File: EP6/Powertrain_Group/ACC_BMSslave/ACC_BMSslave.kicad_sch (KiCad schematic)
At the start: 99 parts, among them IC1 ADBMS1818ASWAZ-R7, J1 Cell taps, J2 Temp probes A, J3 Temp probes B, J4 Temp probes C, J5 Temp probes D, J6 RJ45, J7 RJ45, J8 isoSPI_out, J9 isoSPI_in, U1 LM324DT

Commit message: ACC_BMSslave pcb priliminary layout
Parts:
- C1, C10, C11, C12, C13, C2, C3, C4, C7, C8, C9: footprint Capacitor_SMD:C_0201_0603Metric -> Capacitor_SMD:C_0603_1608Metric
- D1, D2: footprint LED_SMD:LED_0805_2012Metric -> LED_SMD:LED_0603_1608Metric
- R1, R10, R11, R12, R13, R14, R15, R16, R17, R18, R19, R2, R20, R21, R22, R23, R24, R25, R26, R27, R28, R29, R3, R30, R31, R32, R33, R34, R35, R36, R37, R38, R4, R5, R6, R7, R8, R9: footprint Resistor_SMD:R_0603_1608Metric -> Resistor_SMD:R_0402_1005Metric
- U1: footprint Package_SO:SOIC-14-16_3.9x9.9mm_P1.27mm -> Package_SO:SO-14_3.9x8.65mm_P1.27mm
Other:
- note added: "A2,A1,A0 000: T8 001: T7 010: T6 011: T5 100: T1 101: T2 110: T3 111: T4"

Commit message: ACC_BMSslave pcb layout kinda done
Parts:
- removed J1: Cell taps, Connector_JST:JST_XH_B16B-XH-A_1x16_P2.50mm_Vertical, symbol Connector_Generic:Conn_01x16
- added J1: Cell taps A, Connector_JST:JST_XH_B8B-XH-A_1x08_P2.50mm_Vertical, symbol Connector_Generic:Conn_01x08
- added J10: Cell taps B, Connector_JST:JST_XH_B8B-XH-A_1x08_P2.50mm_Vertical, symbol Connector_Generic:Conn_01x08
- C10, C11, C14, C15, C8, C9: footprint Capacitor_SMD:C_0603_1608Metric -> Capacitor_SMD:C_0402_1005Metric
- R33: footprint Resistor_SMD:R_0402_1005Metric -> Resistor_SMD:R_0805_2012Metric
- R34: footprint Resistor_SMD:R_0402_1005Metric -> Resistor_SMD:R_0603_1608Metric
- R39, R46, R47: footprint Resistor_SMD:R_0201_0603Metric -> Resistor_SMD:R_0603_1608Metric
- R40, R41, R42, R43, R44, R45, R48, R49: footprint Resistor_SMD:R_0201_0603Metric -> Resistor_SMD:R_0402_1005Metric
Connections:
- net Earth: now also D1.1 (K); no longer R39.2
- net GPIO6: now also C10.1, R42.2; no longer C8.1, R40.2
- net GPIO7: now also C11.1, R43.2; no longer C9.1, R41.2
- net GPIO8: now also C8.1, R40.2; no longer C10.1, R42.2
- net GPIO9: now also C9.1, R41.2; no longer C11.1, R43.2
- net VREG: now also R39.2; no longer D1.2 (A)
- net tprobe_mux2/OUT: now also U1.12 (+); no longer U1.5 (+)
- net tprobe_mux4/OUT: now also U1.5 (+); no longer U1.12 (+)
- net at F6.1: now also J1.6 (Pin_6)
- net at F10.1: now also J10.2 (Pin_2)
- net at F7.1: now also J1.7 (Pin_7)
- net at F5.1: now also J1.5 (Pin_5)
- net at U1.6 (-), U1.7: now also R43.1; no longer R41.1
- net at F4.1: now also J1.4 (Pin_4)
- net at R39.1: now also D1.2 (A); no longer D1.1 (K)
- net at U1.13 (-), U1.14: now also R41.1; no longer R43.1
- net at F13.1: now also J10.5 (Pin_5)
- net at F11.1: now also J10.3 (Pin_3)
- net at F14.1: now also J10.6 (Pin_6)
- net at F1.1: now also J1.1 (Pin_1)
- net at F12.1: now also J10.4 (Pin_4)
- net at F15.1: now also J10.7 (Pin_7)
- net at F16.1: now also J10.8 (Pin_8)
- net at F2.1: now also J1.2 (Pin_2)
- net at F3.1: now also J1.3 (Pin_3)
- net at F8.1: now also J1.8 (Pin_8)
- net at F9.1: now also J10.1 (Pin_1)
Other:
- moved on the sheet: D1, R39, U1B, U1D

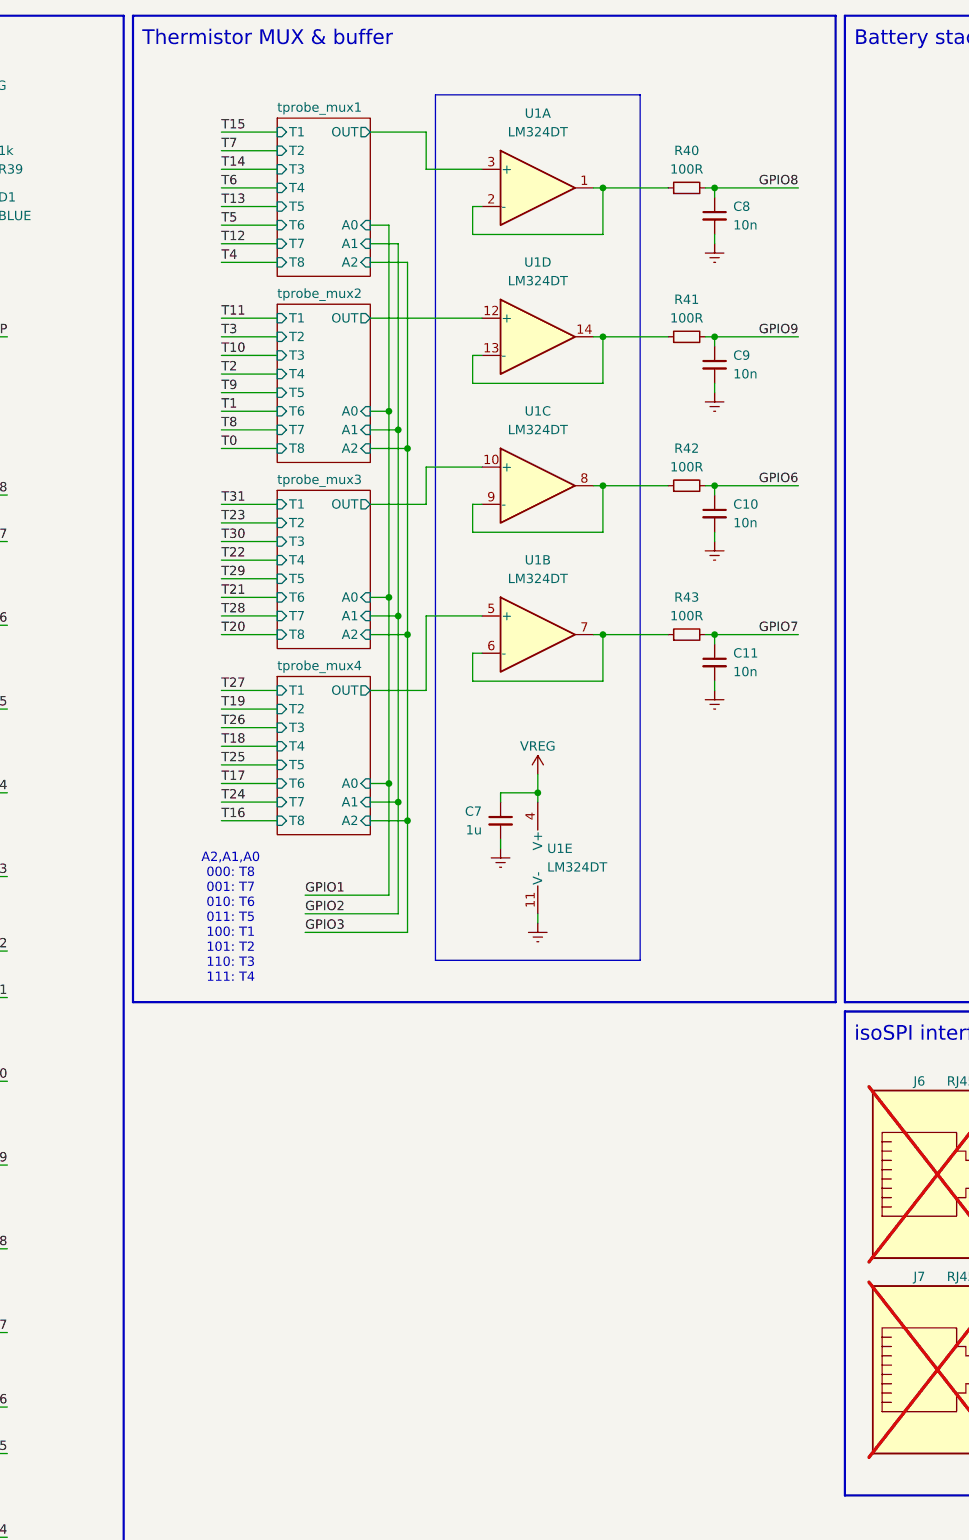
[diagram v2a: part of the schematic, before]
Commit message: ACC_BMSslave optimise layout, added silk
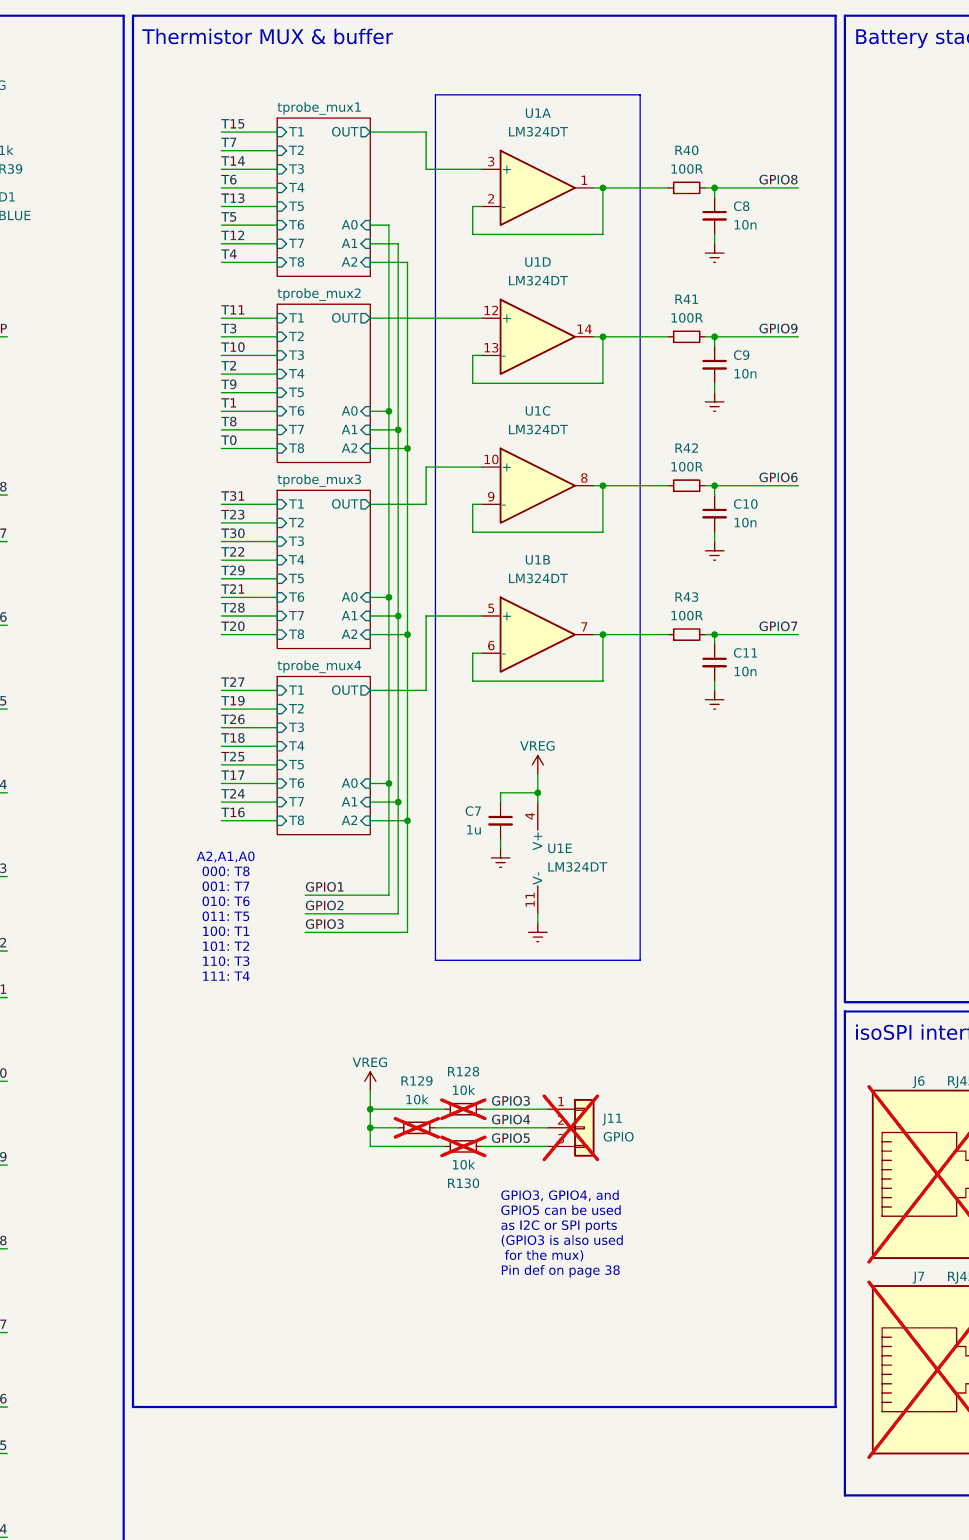
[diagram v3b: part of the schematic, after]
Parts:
- added J11: GPIO, Connector_PinHeader_2.54mm:PinHeader_1x03_P2.54mm_Vertical, symbol Connector_Generic:Conn_01x03
- added R128, R129, R130: 10k, Resistor_SMD:R_0402_1005Metric, symbol Device:R_Small
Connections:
- net GPIO3: now also J11.1 (Pin_1), R128.2
- net GPIO4: now also J11.2 (Pin_2), R129.2
- net GPIO5: now also J11.3 (Pin_3), R130.2
- net VREG: now also R128.1, R129.1, R130.1
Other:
- note added: "GPIO3, GPIO4, and GPIO5 can be used as I2C or SPI ports (GPIO3 is also used for the mux) Pin def on page 38"

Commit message: ACC_BMSslave snapshot
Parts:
- removed D1: BLUE, LED_SMD:LED_0603_1608Metric, symbol Device:LED_Small
- removed J1: Cell taps A, Connector_JST:JST_XH_B8B-XH-A_1x08_P2.50mm_Vertical, symbol Connector_Generic:Conn_01x08
- removed J10: Cell taps B, Connector_JST:JST_XH_B8B-XH-A_1x08_P2.50mm_Vertical, symbol Connector_Generic:Conn_01x08
- removed R31, R32: 10k, Resistor_SMD:R_0402_1005Metric, symbol Device:R_Small
- removed R39: 1k, Resistor_SMD:R_0603_1608Metric, symbol Device:R_Small
- added C26, C57, C58: 10n, Capacitor_SMD:C_0402_1005Metric, symbol Device:C_Small
- added J1: Cell Taps A, Connector_JST:JST_XH_B4B-XH-A_1x04_P2.50mm_Vertical, symbol Connector_Generic:Conn_01x04
- added J10: Cell Taps B, Connector_JST:JST_XH_B4B-XH-A_1x04_P2.50mm_Vertical, symbol Connector_Generic:Conn_01x04
- added J12: Cell Taps C, Connector_JST:JST_XH_B4B-XH-A_1x04_P2.50mm_Vertical, symbol Connector_Generic:Conn_01x04
- added J13: Cell Taps D, Connector_JST:JST_XH_B4B-XH-A_1x04_P2.50mm_Vertical, symbol Connector_Generic:Conn_01x04
- added R131, R132: 100k, Resistor_SMD:R_0402_1005Metric, symbol Device:R_Small
- added R133, R134: 100R, Resistor_SMD:R_0402_1005Metric, symbol Device:R_Small
- added U2: LM324DT, Package_SO:SO-14_3.9x8.65mm_P1.27mm, symbol Amplifier_Operational:LM324
- C11: value 10n -> 1u; footprint Capacitor_SMD:C_0402_1005Metric -> Capacitor_SMD:C_0603_1608Metric
- H1, H2, H3, H4: footprint MountingHole:MountingHole_4.3mm_M4_DIN965 -> MountingHole:MountingHole_3.2mm_M3_DIN965
- R1, R10, R11, R12, R13, R14, R15, R16, R17, R18, R19, R2, R20, R21, R22, R23, R24, R25, R26, R27, R28, R29, R3, R30, R4, R5, R6, R7, R8, R9: value 10k -> 4k3
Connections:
- net T30 is gone; now on net T28: J5.13 (Pin_13)
- net T31 is gone; now on net T29: J5.15 (Pin_15)
- net Earth: now also C26.2, C57.2, C58.2, R131.1, U2.11 (V-)
- net GPIO1: now also C8.1, R40.2
- net GPIO2: now also C9.1, R41.2
- net GPIO7: now also C26.1; no longer C11.1
- net GPIO8: now also C57.1, R133.2; no longer C8.1, R40.2
- net GPIO9: now also C58.1, R134.2; no longer C9.1, R41.2
- net T15: now also J4.1 (Pin_1); no longer J3.15 (Pin_15)
- net T16: now also J4.3 (Pin_3); no longer J4.1 (Pin_1)
- net T17: now also J4.5 (Pin_5); no longer J4.3 (Pin_3)
- net T18: now also J4.7 (Pin_7); no longer J4.5 (Pin_5)
- net T19: now also J4.9 (Pin_9); no longer J4.7 (Pin_7)
- net T20: now also J4.11 (Pin_11); no longer J4.9 (Pin_9)
- net T21: now also J4.13 (Pin_13); no longer J4.11 (Pin_11)
- net T22: now also J5.1 (Pin_1); no longer J4.13 (Pin_13)
- net T23: now also J5.3 (Pin_3); no longer J4.15 (Pin_15)
- net T24: now also J5.5 (Pin_5); no longer J5.1 (Pin_1)
- net T25: now also J5.7 (Pin_7); no longer J5.3 (Pin_3)
- net T26: now also J5.9 (Pin_9); no longer J5.5 (Pin_5)
- net T27: now also J5.11 (Pin_11); no longer J5.7 (Pin_7)
- net T28: no longer J5.9 (Pin_9)
- net T29: no longer J5.11 (Pin_11)
- net VREG: now also C11.1, R132.2, U2.4 (V+)
- net tprobe_mux4/OUT: now also U2.3 (+); no longer U1.5 (+)
- net at F6.1: now also J10.2 (Pin_2)
- net at F10.1: now also J12.2 (Pin_2)
- net at F7.1: now also J10.3 (Pin_3)
- net at F9.1: now also J12.1 (Pin_1)
- net at F11.1: now also J12.3 (Pin_3)
- net at F12.1: now also J12.4 (Pin_4)
- net at F13.1: now also J13.1 (Pin_1)
- net at F14.1: now also J13.2 (Pin_2)
- net at F15.1: now also J13.3 (Pin_3)
- net at F16.1: now also J13.4 (Pin_4)
- net at F5.1: now also J10.1 (Pin_1)
- net at U1.6 (-), U1.7: no longer R43.1
- net at F4.1: now also J1.4 (Pin_4)
- net at F3.1: now also J1.3 (Pin_3)
- net at F8.1: now also J10.4 (Pin_4)
- net at F1.1: now also J1.1 (Pin_1)
- net at F2.1: now also J1.2 (Pin_2)
- new net: R133.1, U2.13 (-), U2.14
- new net: U2.6 (-), U2.7
- new net: R134.1, U2.8, U2.9 (-)
- new net: R43.1, U2.1, U2.2 (-)
- new net mid_supply: R131.2, R132.1, U1.5 (+), U2.5 (+)
- new net tprobe_mux5/OUT: U2.12 (+)
- new net tprobe_mux6/OUT: U2.10 (+)
- no-connect marks 19 -> 39
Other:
- added sheet tprobe_mux5 (tprobe_mux.kicad_sch)
- added sheet tprobe_mux6 (tprobe_mux.kicad_sch)
- note added: "GPIO3, GPIO4, and GPIO5 can be used as I2C or SPI ports Pin def on page 38"
- note removed: "GPIO3, GPIO4, and GPIO5 can be used as I2C or SPI ports (GPIO3 is also used for the mux) Pin def on page 38"
- moved on the sheet: C7, J11, R128, R129, R130, R16, R17, R18, R19, R20, R21, R22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

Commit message: ACC_BMSslave snapshot
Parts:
- removed C11: 1u, Capacitor_SMD:C_0603_1608Metric, symbol Device:C_Small
- removed C26, C58: 10n, Capacitor_SMD:C_0402_1005Metric, symbol Device:C_Small
- removed R131, R132: 100k, Resistor_SMD:R_0402_1005Metric, symbol Device:R_Small
- removed R133, R134, R43: 100R, Resistor_SMD:R_0402_1005Metric, symbol Device:R_Small
- removed U2: LM324DT, Package_SO:SO-14_3.9x8.65mm_P1.27mm, symbol Amplifier_Operational:LM324
- added R31, R32: 4k3, Resistor_SMD:R_0402_1005Metric, symbol Device:R_Small
- added R39: 100R, Resistor_SMD:R_0402_1005Metric, symbol Device:R_Small
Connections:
- net mid_supply is gone; now on net tprobe_mux4/OUT: U1.5 (+)
- net GPIO1: no longer C8.1, R40.2
- net GPIO2: no longer C9.1, R41.2
- net GPIO6: now also C8.1, R40.2; no longer C10.1, R42.2
- net GPIO7: now also C9.1, R41.2
- net GPIO8: now also R39.2
- net GPIO9: now also C10.1, R42.2
- net T15: now also J3.15 (Pin_15); no longer J4.1 (Pin_1)
- net T16: now also J4.1 (Pin_1); no longer J4.3 (Pin_3)
- net T17: now also J4.3 (Pin_3); no longer J4.5 (Pin_5)
- net T18: now also J4.5 (Pin_5); no longer J4.7 (Pin_7)
- net T19: now also J4.7 (Pin_7); no longer J4.9 (Pin_9)
- net T20: now also J4.9 (Pin_9); no longer J4.11 (Pin_11)
- net T21: now also J4.11 (Pin_11); no longer J4.13 (Pin_13)
- net T22: now also J4.13 (Pin_13); no longer J5.1 (Pin_1)
- net T23: now also J4.15 (Pin_15); no longer J5.3 (Pin_3)
- net T24: now also J5.1 (Pin_1); no longer J5.5 (Pin_5)
- net T25: now also J5.3 (Pin_3); no longer J5.7 (Pin_7)
- net T26: now also J5.5 (Pin_5); no longer J5.9 (Pin_9)
- net T27: now also J5.7 (Pin_7); no longer J5.11 (Pin_11)
- net T28: now also J5.9 (Pin_9); no longer J5.13 (Pin_13)
- net T29: now also J5.11 (Pin_11); no longer J5.15 (Pin_15)
- net VREF2: now also R31.2, R32.2
- net tprobe_mux1/OUT: now also U1.12 (+); no longer U1.3 (+)
- net tprobe_mux2/OUT: now also U1.3 (+); no longer U1.12 (+)
- net at U1.1, U1.2 (-): now also R41.1; no longer R40.1
- net at U1.6 (-), U1.7: now also R39.1
- net at U1.13 (-), U1.14: now also R40.1; no longer R41.1
- new net T30: J5.13 (Pin_13), R31.1
- new net T31: J5.15 (Pin_15), R32.1
- no-connect marks 39 -> 19
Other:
- removed sheet tprobe_mux5
- removed sheet tprobe_mux6
- moved on the sheet: R16, R17, R18, R19, R20, R21, R22, R23, R24, R25, R26, R27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

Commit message: [BMSslave] snapshot
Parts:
- removed C1, C2, C3, C4: 100n, Capacitor_SMD:C_0603_1608Metric, symbol Device:C_Small
- removed J1: Cell Taps A, Connector_JST:JST_XH_B4B-XH-A_1x04_P2.50mm_Vertical, symbol Connector_Generic:Conn_01x04
- removed J10: Cell Taps B, Connector_JST:JST_XH_B4B-XH-A_1x04_P2.50mm_Vertical, symbol Connector_Generic:Conn_01x04
- removed J12: Cell Taps C, Connector_JST:JST_XH_B4B-XH-A_1x04_P2.50mm_Vertical, symbol Connector_Generic:Conn_01x04
- removed J13: Cell Taps D, Connector_JST:JST_XH_B4B-XH-A_1x04_P2.50mm_Vertical, symbol Connector_Generic:Conn_01x04
- removed J2: Temp probes A, Connector_JST:JST_PH_B16B-PH-K_1x16_P2.00mm_Vertical, symbol Connector_Generic:Conn_01x16
- removed J3: Temp probes B, Connector_JST:JST_PH_B16B-PH-K_1x16_P2.00mm_Vertical, symbol Connector_Generic:Conn_01x16
- removed J5: Temp probes D, Connector_JST:JST_PH_B16B-PH-K_1x16_P2.00mm_Vertical, symbol Connector_Generic:Conn_01x16
- removed R1, R10, R11, R12, R13, R14, R15, R16, R17, R18, R19, R2, R20, R21, R22, R23, R24, R25, R26, R27, R28, R29, R3, R30, R31, R32, R4, R5, R6, R7, R8, R9: 4k3, Resistor_SMD:R_0402_1005Metric, symbol Device:R_Small
- added J1: B2B_CELL_TAPS_1, Connector_PinHeader_2.54mm:PinHeader_1x16_P2.54mm_Vertical, symbol Connector_Generic:Conn_01x16
- added J2: B2B_NTC_1, Connector_PinHeader_2.54mm:PinHeader_1x10_P2.54mm_Vertical, symbol Connector_Generic:Conn_01x10
- added J3: B2B_NTC_2, Connector_PinHeader_2.54mm:PinHeader_1x10_P2.54mm_Vertical, symbol Connector_Generic:Conn_01x10
- added J5: B2B_NTC_3, Connector_PinHeader_2.54mm:PinHeader_1x10_P2.54mm_Vertical, symbol Connector_Generic:Conn_01x10
- added J6: B2B_NTC_4, Connector_PinHeader_2.54mm:PinHeader_1x10_P2.54mm_Vertical, symbol Connector_Generic:Conn_01x10
- J4: value Temp probes C -> B2B_CELL_TAPS_2; footprint Connector_JST:JST_PH_B16B-PH-K_1x16_P2.00mm_Vertical -> Connector_PinHeader_2.54mm:PinHeader_1x16_P2.54mm_Vertical
- renumbered C5 to C1, C14 to C10, C15 to C11, C16 to C12, C6 to C2, C7 to C3, C8 to C4, C9 to C5, C10 to C6, C57 to C7, C12 to C8, C13 to C9, D2 to D1, J8 to J10, J9 to J11, J11 to J7, J6 to J8, J7 to J9, R33 to R1, R40 to R10, R41 to R11, R42 to R12, R39 to R13, R44 to R14, R45 to R15, R46 to R16, R47 to R17, R48 to R18, R49 to R19, R34 to R2, R35 to R3, R36 to R4, R37 to R5, R38 to R6, R129 to R7, R128 to R8, R130 to R9
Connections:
- net Earth: now also J2.3 (Pin_3), J2.8 (Pin_8), J3.3 (Pin_3), J3.8 (Pin_8), J5.3 (Pin_3), J5.8 (Pin_8), J6.3 (Pin_3), J6.8 (Pin_8); no longer J4.10 (Pin_10), J4.12 (Pin_12), J4.14 (Pin_14), J4.16 (Pin_16), J4.2 (Pin_2), J4.4 (Pin_4), J4.6 (Pin_6), J4.8 (Pin_8)
- net T0: now also J2.1 (Pin_1)
- net T1: now also J2.2 (Pin_2)
- net T10: now also J3.4 (Pin_4)
- net T11: now also J3.5 (Pin_5)
- net T12: now also J3.6 (Pin_6)
- net T13: now also J3.7 (Pin_7)
- net T14: now also J3.9 (Pin_9)
- net T15: now also J3.10 (Pin_10)
- net T16: now also J5.1 (Pin_1); no longer J4.1 (Pin_1)
- net T17: now also J5.2 (Pin_2); no longer J4.3 (Pin_3)
- net T18: now also J5.4 (Pin_4); no longer J4.5 (Pin_5)
- net T19: now also J5.5 (Pin_5); no longer J4.7 (Pin_7)
- net T2: now also J2.4 (Pin_4)
- net T20: now also J5.6 (Pin_6); no longer J4.9 (Pin_9)
- net T21: now also J5.7 (Pin_7); no longer J4.11 (Pin_11)
- net T22: now also J5.9 (Pin_9); no longer J4.13 (Pin_13)
- net T23: now also J5.10 (Pin_10); no longer J4.15 (Pin_15)
- net T24: now also J6.1 (Pin_1)
- net T25: now also J6.2 (Pin_2)
- net T26: now also J6.4 (Pin_4)
- net T27: now also J6.5 (Pin_5)
- net T28: now also J6.6 (Pin_6)
- net T29: now also J6.7 (Pin_7)
- net T3: now also J2.5 (Pin_5)
- net T30: now also J6.9 (Pin_9)
- net T31: now also J6.10 (Pin_10)
- net T4: now also J2.6 (Pin_6)
- net T5: now also J2.7 (Pin_7)
- net T6: now also J2.9 (Pin_9)
- net T7: now also J2.10 (Pin_10)
- net T8: now also J3.1 (Pin_1)
- net T9: now also J3.2 (Pin_2)
- net tprobe_mux1/OUT: now also U1.3 (+); no longer U1.12 (+)
- net tprobe_mux2/OUT: now also U1.12 (+); no longer U1.3 (+)
- net tprobe_mux3/OUT: now also U1.5 (+); no longer U1.10 (+)
- net tprobe_mux4/OUT: now also U1.10 (+); no longer U1.5 (+)
- net at F13.1: now also J4.13 (Pin_13), J1.13 (Pin_13)
- net at F14.1: now also J4.14 (Pin_14), J1.14 (Pin_14)
- net at F15.1: now also J4.15 (Pin_15), J1.15 (Pin_15)
- net at F16.1: now also J4.16 (Pin_16), J1.16 (Pin_16)
- net at F9.1: now also J4.9 (Pin_9), J1.9 (Pin_9)
- net at F10.1: now also J4.10 (Pin_10), J1.10 (Pin_10)
- net at F11.1: now also J4.11 (Pin_11), J1.11 (Pin_11)
- net at F12.1: now also J4.12 (Pin_12), J1.12 (Pin_12)
- net at F6.1: now also J4.6 (Pin_6), J1.6 (Pin_6)
- net at U1.1, U1.2 (-): now also R13.1; no longer R11.1
- net at F1.1: now also J4.1 (Pin_1), J1.1 (Pin_1)
- net at F2.1: now also J4.2 (Pin_2), J1.2 (Pin_2)
- net at F3.1: now also J4.3 (Pin_3), J1.3 (Pin_3)
- net at F4.1: now also J4.4 (Pin_4), J1.4 (Pin_4)
- net at F7.1: now also J4.7 (Pin_7), J1.7 (Pin_7)
- net at F5.1: now also J4.5 (Pin_5), J1.5 (Pin_5)
- net at U1.6 (-), U1.7: now also R12.1; no longer R13.1
- net at F8.1: now also J4.8 (Pin_8), J1.8 (Pin_8)
- net at U1.8, U1.9 (-): now also R11.1; no longer R12.1
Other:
- sheet tprobe_mux1 ports: added VREF; removed none
- sheet tprobe_mux2 ports: added VREF; removed none
- sheet tprobe_mux3 ports: added VREF; removed none
- sheet tprobe_mux4 ports: added VREF; removed none
- moved on the sheet: F1, F10, F11, F12, F13, F14, F15, F16, F2, F3, F4, F5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
